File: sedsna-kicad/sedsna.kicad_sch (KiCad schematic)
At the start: 33 parts, among them J5 USB4105-GF-A, U2 ESP32-C3, U4 Magnetometer, U5 IMU, U6 LDL1117S33R

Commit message: Added connectors/antenna
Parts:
- added C8, C9: 1.2pF, symbol Device:C
- added J3: Servos_Rudder/Elevator, symbol Connector_Generic:Conn_02x03_Counter_Clockwise
- added J4: L_Aileron, symbol Connector_Generic:Conn_01x03
- added J6: R_Aileron, symbol Connector_Generic:Conn_01x03
- added J7: Prop, symbol Connector_Generic:Conn_01x03
- added J8: Antenna, symbol Connector:Conn_Coaxial_Small
- added L1: 2nH, symbol Device:L
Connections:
- net Earth: now also C8.2, C9.2, J3.3 (Pin_3), J3.4 (Pin_4), J4.1 (Pin_1), J6.1 (Pin_1), J7.1 (Pin_1), J8.2 (Ext); no longer U2.1 (LNA_IN)
- net +7.4V: now reaches BR1.1, C4.1, C5.2, FB1.2, U6.3 (VIN)
- net +7.4V: now also J3.2 (Pin_2), J3.5 (Pin_5), J4.2 (Pin_2), J6.2 (Pin_2)
- net CTR_R_Ail: now reaches U2.10 (MTDI)
- net CTR_R_Ail: now also J6.3 (Pin_3)
- net CTR_Rudder: now reaches U2.12 (MTCK)
- net CTR_Rudder: now also J3.6 (Pin_6)
- net CTR_Elevator: now reaches U2.13 (MTDO)
- net CTR_Elevator: now also J3.1 (Pin_1)
- net CTR_Prop: now reaches U2.8 (GPIO3)
- net CTR_Prop: now also J7.3 (Pin_3)
- net CTR_L_Ail: now reaches U2.9 (MTMS)
- net CTR_L_Ail: now also J4.3 (Pin_3)
- new net: C8.1, J8.1 (In), L1.2
- new net ANT: C9.1, L1.1, U2.1 (LNA_IN)
- no-connect marks 11 -> 12
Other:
- note added: "Antenna"
- note added: "Connectors"

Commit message: footprints are footprinting
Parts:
- C1, C2: footprint (none) -> Capacitor_SMD:C_0402_1005Metric_Pad0.74x0.62mm_HandSolder
- C7: footprint (none) -> Capacitor_SMD:C_01005_0402Metric_Pad0.57x0.30mm_HandSolder
- C8, C9: footprint (none) -> Capacitor_SMD:C_0201_0603Metric_Pad0.64x0.40mm_HandSolder
- L1: footprint (none) -> Inductor_SMD:L_0402_1005Metric_Pad0.77x0.64mm_HandSolder
- R2: footprint (none) -> Resistor_SMD:R_0603_1608Metric_Pad0.98x0.95mm_HandSolder
- U2: footprint QFN32_5X5_EXP -> (none)
- XTAL1: footprint ECX-1637B2_ECS -> (none)
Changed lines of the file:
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@@
 			)
 		)
-		(property "Footprint" ""
+		(property "Footprint" "Capacitor_SMD:C_0201_0603Metric_Pad0.64x0.40mm_HandSolder"
 			(at 315.9252 99.06 0)
 			(hide yes)
@@
 			)
 		)
-		(property "Footprint" ""
+		(property "Footprint" "Resistor_SMD:R_0603_1608Metric_Pad0.98x0.95mm_HandSolder"
 			(at 141.224 124.206 90)
 			(hide yes)
@@
 			)
 		)
-		(property "Footprint" ""
+		(property "Footprint" "Capacitor_SMD:C_0402_1005Metric_Pad0.74x0.62mm_HandSolder"
 			(at 206.7052 127 0)
 			(hide yes)
@@
 			)
 		)
-		(property "Footprint" ""
+		(property "Footprint" "Capacitor_SMD:C_01005_0402Metric_Pad0.57x0.30mm_HandSolder"
 			(at 276.5552 99.06 0)
 			(hide yes)
@@
 			)
 		)
-		(property "Footprint" "QFN32_5X5_EXP"
+		(property "Footprint" ""
 			(at 69.85 129.54 0)
 			(hide yes)
@@
 			)
 		)
-		(property "Footprint" ""
+		(property "Footprint" "Capacitor_SMD:C_0201_0603Metric_Pad0.64x0.40mm_HandSolder"
 			(at 332.4352 99.06 0)
 			(hide yes)
@@
 			)
 		)
-		(property "Footprint" ""
+		(property "Footprint" "Inductor_SMD:L_0402_1005Metric_Pad0.77x0.64mm_HandSolder"
 			(at 323.85 85.09 0)
 			(hide yes)
@@
 			)
 		)
-		(property "Footprint" ""
+		(property "Footprint" "Capacitor_SMD:C_0402_1005Metric_Pad0.74x0.62mm_HandSolder"
 			(at 154.6352 127 0)
 			(hide yes)
@@
 			)
 		)
-		(property "Footprint" "ECX-1637B2_ECS"
+		(property "Footprint" ""
 			(at 154.94 119.38 0)
 			(hide yes)

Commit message: library shit
aa
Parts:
- J3: footprint (none) -> sedsna:CONN06_2035551016_MOL
- U2: footprint (none) -> Connector_Coaxial:SMA_Molex_73251-1153_EdgeMount_Horizontal
- U4: footprint (none) -> TR3_V1:MAGNETO-MLX90395KDC
- XTAL1: footprint (none) -> TR3_V1:XTAL_ECS-400-10-37B2-CKY-TR
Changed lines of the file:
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@@
 			)
 		)
-		(property "Footprint" ""
+		(property "Footprint" "Connector_Coaxial:SMA_Molex_73251-1153_EdgeMount_Horizontal"
 			(at 69.85 129.54 0)
 			(hide yes)
@@
 			)
 		)
-		(property "Footprint" ""
+		(property "Footprint" "sedsna:CONN06_2035551016_MOL"
 			(at 287.02 147.32 0)
 			(hide yes)
@@
 			)
 		)
-		(property "Footprint" ""
+		(property "Footprint" "TR3_V1:MAGNETO-MLX90395KDC"
 			(at 255.27 93.98 0)
 			(hide yes)
@@
 			)
 		)
-		(property "Footprint" ""
+		(property "Footprint" "TR3_V1:XTAL_ECS-400-10-37B2-CKY-TR"
 			(at 154.94 119.38 0)
 			(hide yes)

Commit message: all footprints
raaa
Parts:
- J4, J6, J7: footprint (none) -> sedsna:CONN_SDA_42002-xxxxx_03_MOL
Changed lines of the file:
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@@
 			)
 		)
-		(property "Footprint" ""
+		(property "Footprint" "sedsna:CONN_SDA_42002-xxxxx_03_MOL"
 			(at 262.89 153.67 0)
 			(hide yes)
@@
 			)
 		)
-		(property "Footprint" ""
+		(property "Footprint" "sedsna:CONN_SDA_42002-xxxxx_03_MOL"
 			(at 242.57 153.67 0)
 			(hide yes)
@@
 			)
 		)
-		(property "Footprint" ""
+		(property "Footprint" "sedsna:CONN_SDA_42002-xxxxx_03_MOL"
 			(at 252.73 153.67 0)
 			(hide yes)

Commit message: added antenna sma footprint
142-0701-801 https://www.digikey.com/en/products/detail/cinch-connectivity-solutions-johnson/142-0701-801/35280
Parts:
- J8: footprint (none) -> sedsna:CONN_142-0701-801
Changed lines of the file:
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@@
 			)
 		)
-		(property "Footprint" ""
+		(property "Footprint" "sedsna:CONN_142-0701-801"
 			(at 342.9 96.52 0)
 			(hide yes)

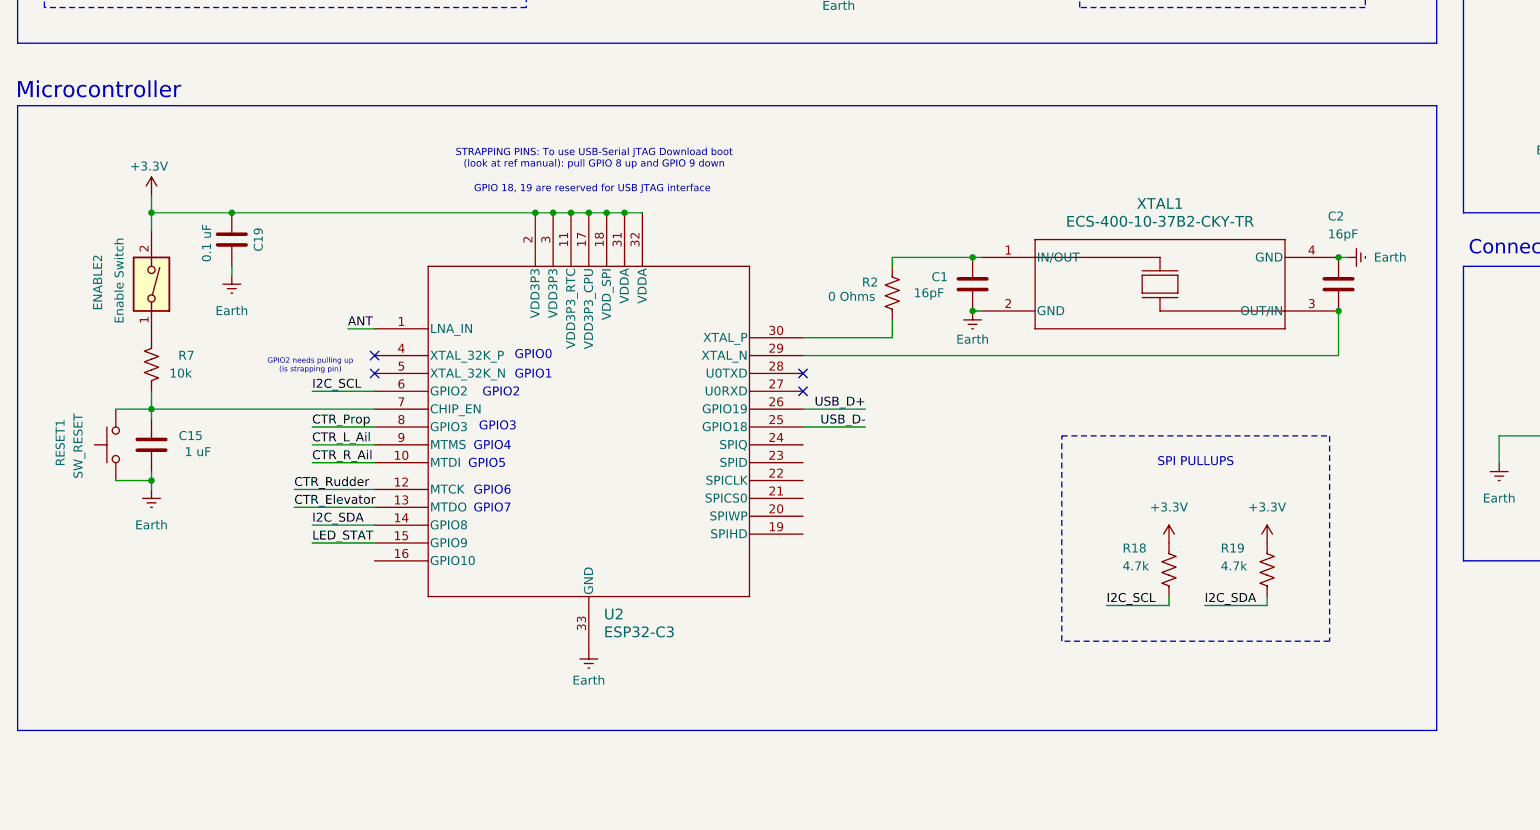
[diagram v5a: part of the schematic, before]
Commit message: added status led
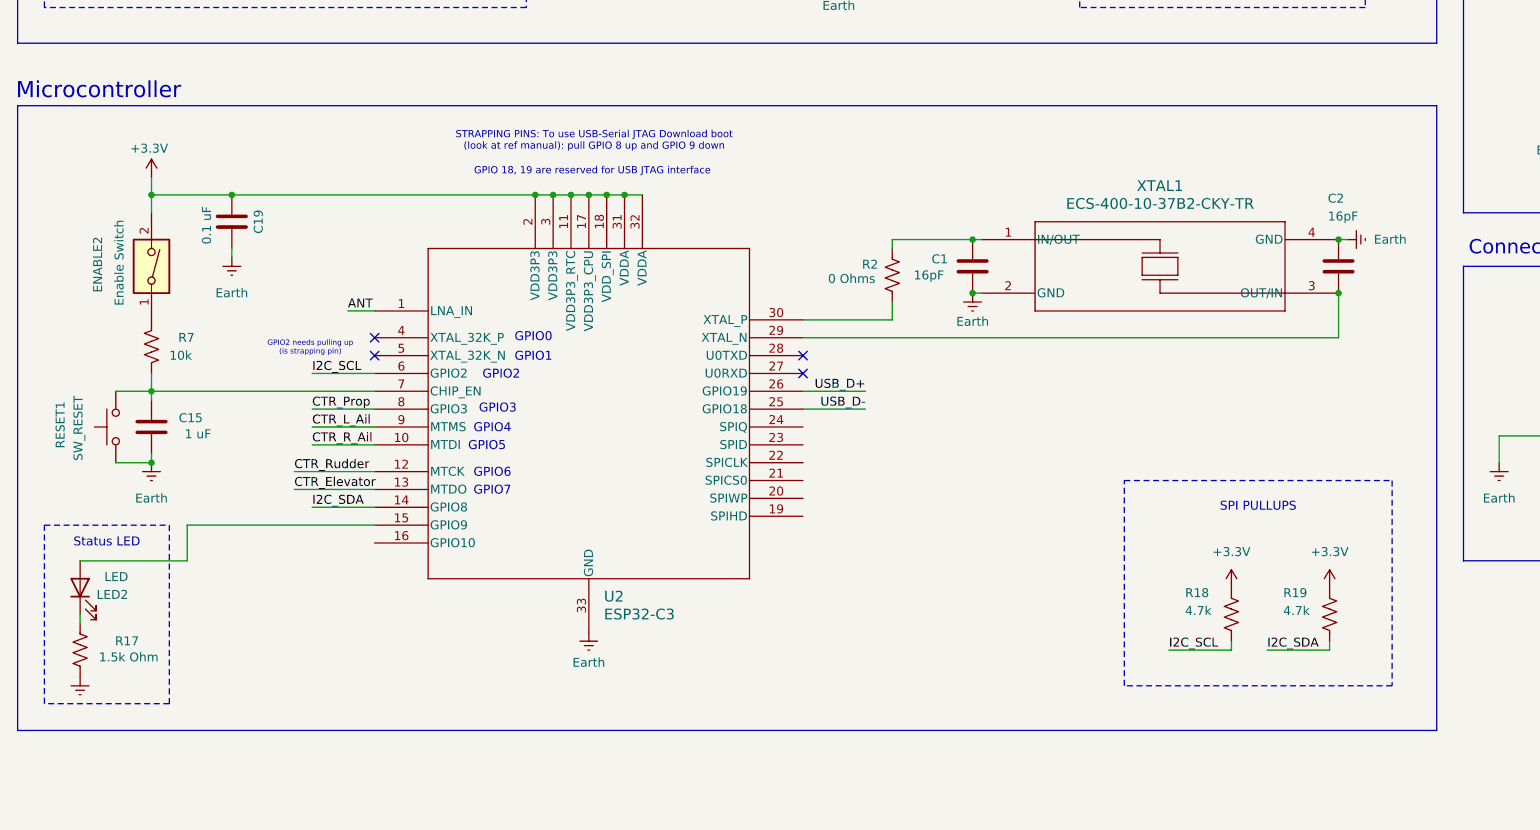
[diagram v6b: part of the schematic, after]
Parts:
- added LED2: LED, TR3_V1:150080RS75000_WRE, symbol TR3_V1:LED
- added R17: 1.5k Ohm, Resistor_SMD:R_0603_1608Metric_Pad0.98x0.95mm_HandSolder, symbol TR3_V1:R_US
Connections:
- net Earth: now also R17.2
- net LED_STAT: no longer names the net of U2.15 (GPIO9)
- net LED_STAT: now also LED2.2 (A)
- new net: LED2.1 (K), R17.1
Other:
- note added: "Status LED"
- moved on the sheet: C1, C15, C19, C2, ENABLE2, R18, R19, R2, R7, RESET1, U2, XTAL1

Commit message: pins added
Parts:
- removed LED2: LED, TR3_V1:150080RS75000_WRE, symbol TR3_V1:LED
- removed R17: 1.5k Ohm, Resistor_SMD:R_0603_1608Metric_Pad0.98x0.95mm_HandSolder, symbol TR3_V1:R_US
- added J1, J10, J2, J9: Conn_01x03, symbol Connector_Generic:Conn_01x03
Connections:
- net +3.3V: now also J1.1 (Pin_1), J10.1 (Pin_1), J2.1 (Pin_1), J9.1 (Pin_1)
- net LED_STAT: now reaches U2.15 (GPIO9)
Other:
- note removed: "Status LED"
- moved on the sheet: C1, C15, C19, C2, ENABLE2, R18, R19, R2, R7, RESET1, U2, XTAL1

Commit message: some ERC errors fixed
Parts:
- added R17: 1.5k Ohm, Resistor_SMD:R_0603_1608Metric_Pad0.98x0.95mm_HandSolder, symbol TR3_V1:R_US
- added STAT1: LED, TR3_V1:150080RS75000_WRE, symbol TR3_V1:LED
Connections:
- net Earth: now also R17.2
- net at U2.28 (U0TXD): now also STAT1.2 (A)
- net LED_STAT: no longer names the net of U2.15 (GPIO9)
- new net: R17.1, STAT1.1 (K)
- no-connect marks 12 -> 17
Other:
- note added: "STATUS LED"
